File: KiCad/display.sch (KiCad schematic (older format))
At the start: 48 parts, among them IC6 PCA9517ADP, J1 46756-1001, T1 BSS138APW, U6 TPD4E05U06QDQARQ1, U7 TPD4E05U06QDQARQ1

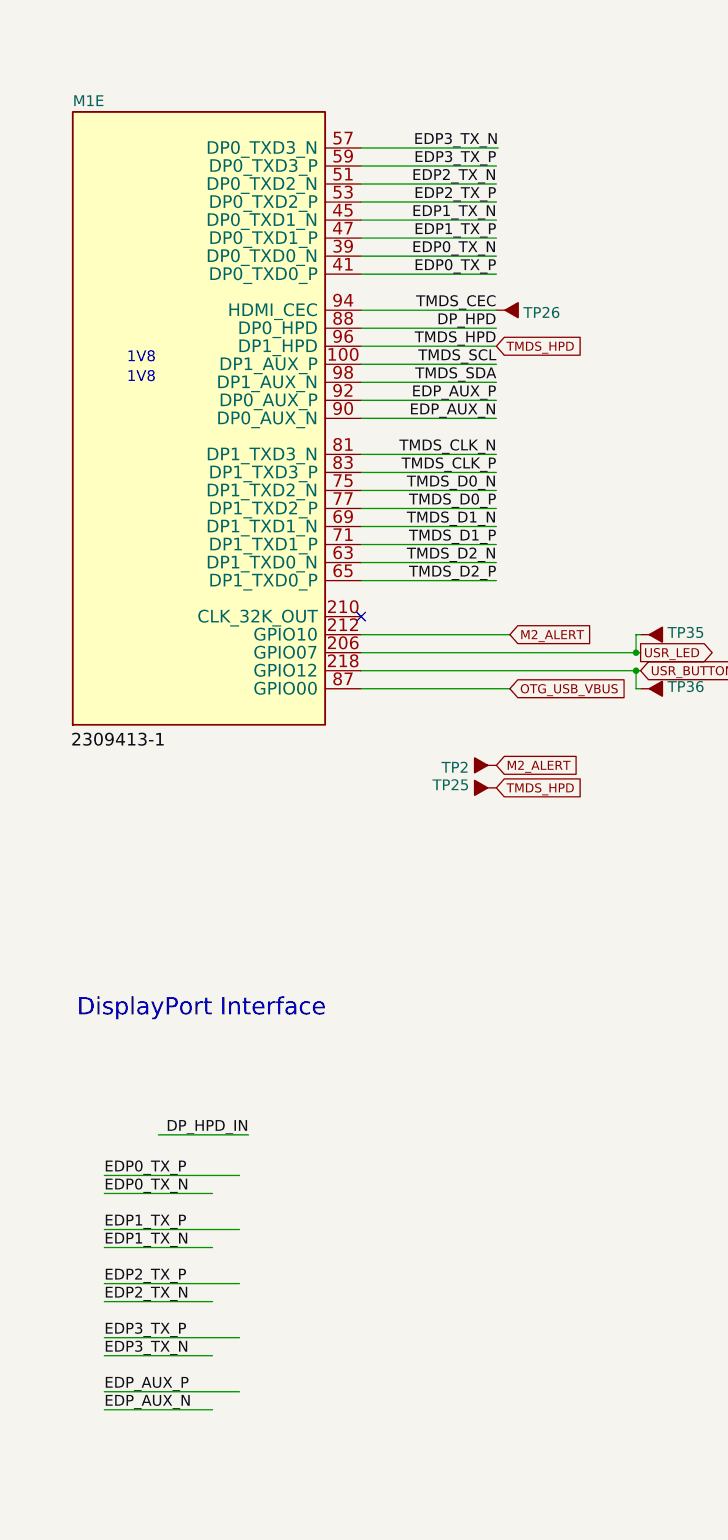
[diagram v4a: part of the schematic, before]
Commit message: Add global labels for DP/HDMI signals
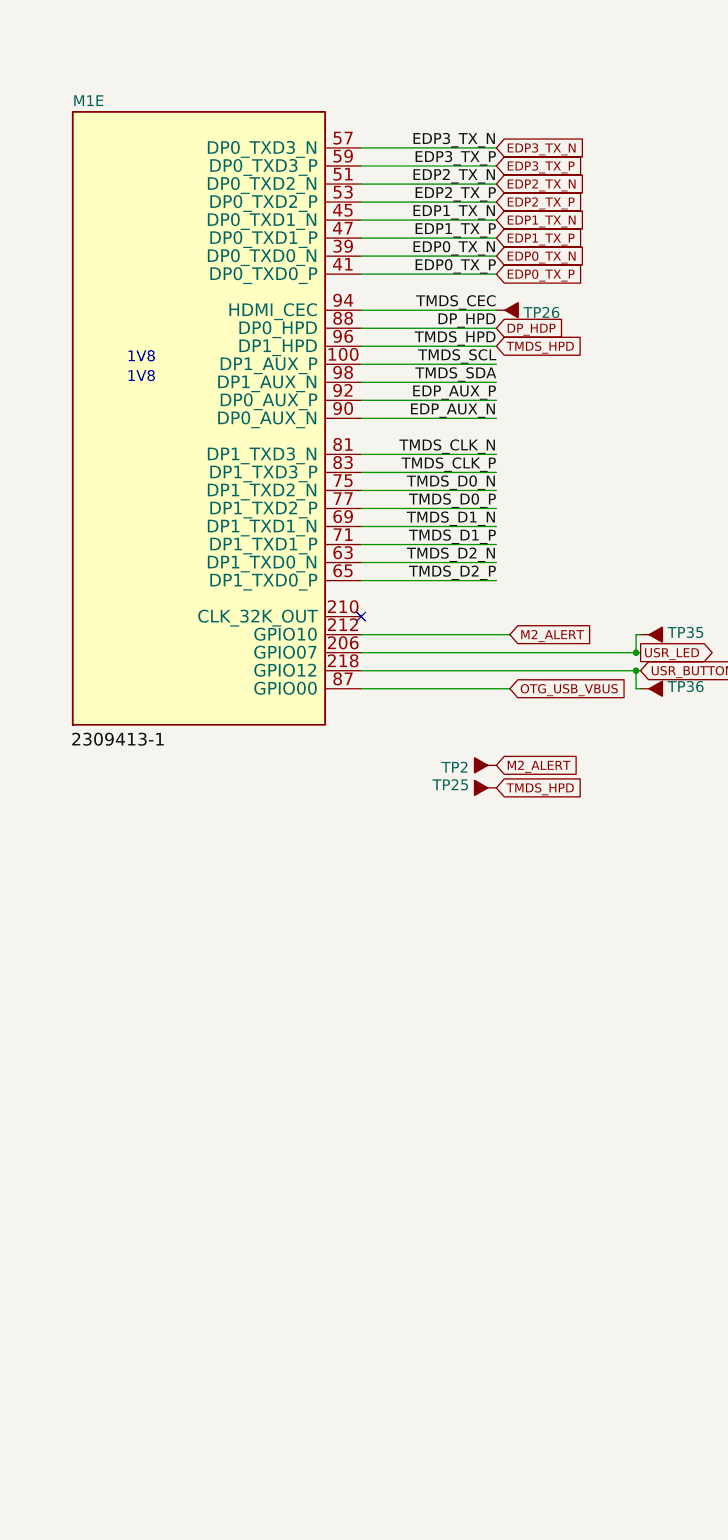
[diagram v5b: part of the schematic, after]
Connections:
- net labels added: DP_HDP
- net labels removed: DP_HPD_IN
- wire segments 191 -> 180
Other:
- note removed: "DisplayPort Interface"
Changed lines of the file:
@@
 Text Label 3250 2500 2    60   ~ 0
 EDP0_TX_P
-Text Label 3260 1800 2    60   ~ 0
-EDP3_TX_N
-Wire Wire Line
-	2500 1800 3260 1800
-Wire Wire Line
-	2500 1900 3250 1900
-Wire Wire Line
-	2500 2000 3250 2000
-Wire Wire Line
-	2500 2100 3250 2100
-Wire Wire Line
-	2500 2200 3250 2200
-Wire Wire Line
-	2500 2300 3250 2300
-Wire Wire Line
-	2500 2400 3250 2400
-Wire Wire Line
-	2500 2500 3250 2500
 Wire Wire Line
 	2500 2800 3250 2800
@@
 	0    1    1    0
 $EndComp
-Text Notes 923  6628 0    96   ~ 0
-DisplayPort Interface
 $Comp
 L jetson-nano-baseboard:46756-1001 J1
@@
 Text GLabel 11275 7575 1    50   Input ~ 0
 3V3_SYS
-Wire Wire Line
-	1675 8800 1075 8800
-Wire Wire Line
-	1675 8500 1075 8500
-Wire Wire Line
-	1675 8200 1075 8200
-Wire Wire Line
-	1675 7900 1075 7900
-Wire Wire Line
-	1675 7600 1075 7600
-Wire Wire Line
-	1825 8700 1075 8700
-Wire Wire Line
-	1825 8400 1075 8400
-Wire Wire Line
-	1825 8100 1075 8100
-Wire Wire Line
-	1825 7800 1075 7800
-Wire Wire Line
-	1825 7500 1075 7500
-Text Label 1075 7500 0    60   ~ 0
-EDP0_TX_P
-Text Label 1075 7600 0    60   ~ 0
-EDP0_TX_N
-Text Label 1075 7800 0    60   ~ 0
-EDP1_TX_P
-Text Label 1075 7900 0    60   ~ 0
-EDP1_TX_N
-Text Label 1075 8700 0    60   ~ 0
-EDP_AUX_P
-Text Label 1075 8800 0    60   ~ 0
-EDP_AUX_N
-Text Label 1075 8100 0    60   ~ 0
-EDP2_TX_P
-Text Label 1075 8200 0    60   ~ 0
-EDP2_TX_N
-Text Label 1075 8400 0    60   ~ 0
-EDP3_TX_P
-Text Label 1075 8500 0    60   ~ 0
-EDP3_TX_N
 Text Label 4750 3450 0    60   ~ 0
 TMDS_CLK_N
@@
 Text Label 14750 9000 2    60   ~ 0
 TMDS_CEC_GND
-Text Label 1875 7275 2    60   ~ 0
-DP_HPD_IN
-Wire Wire Line
-	1375 7275 1875 7275
+Wire Wire Line
+	2500 1800 3250 1800
+Text Label 3250 1800 2    60   ~ 0
+EDP3_TX_N
+Wire Wire Line
+	2500 1900 3250 1900
+Wire Wire Line
+	2500 2000 3250 2000
+Wire Wire Line
+	2500 2100 3250 2100
+Wire Wire Line
+	2500 2200 3250 2200
+Wire Wire Line
+	2500 2300 3250 2300
+Wire Wire Line
+	2500 2400 3250 2400
+Wire Wire Line
+	2500 2500 3250 2500
+Text GLabel 3250 1800 2    50   Input ~ 0
+EDP3_TX_N
+Text GLabel 3250 1900 2    50   Input ~ 0
+EDP3_TX_P
+Text GLabel 3250 2000 2    50   Input ~ 0
+EDP2_TX_N
+Text GLabel 3250 2100 2    50   Input ~ 0
+EDP2_TX_P
+Text GLabel 3250 2200 2    50   Input ~ 0
+EDP1_TX_N
+Text GLabel 3250 2300 2    50   Input ~ 0
+EDP1_TX_P
+Text GLabel 3250 2400 2    50   Input ~ 0
+EDP0_TX_N
+Text GLabel 3250 2500 2    50   Input ~ 0
+EDP0_TX_P
+Text GLabel 3250 2800 2    50   Input ~ 0
+DP_HDP
 $EndSCHEMATC
